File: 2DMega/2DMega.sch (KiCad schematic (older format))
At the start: 41 parts, among them J1 Conn_01x06_Male, J2 Conn_01x06_Female, J3 Conn_02x03_Odd_Even, J4 Conn_01x06_Male, J5 Conn_01x06_Female, P1 Power, P10 CONN_01X01, P11 CONN_01X01, P12 CONN_01X01, P13 CONN_01X01, P2 Analog, P3 Analog, P4 Digital, P5 PWM, P6 PWM, P7 Communication, P8 CONN_01X01, P9 CONN_01X01, U1 SC39-11YWA

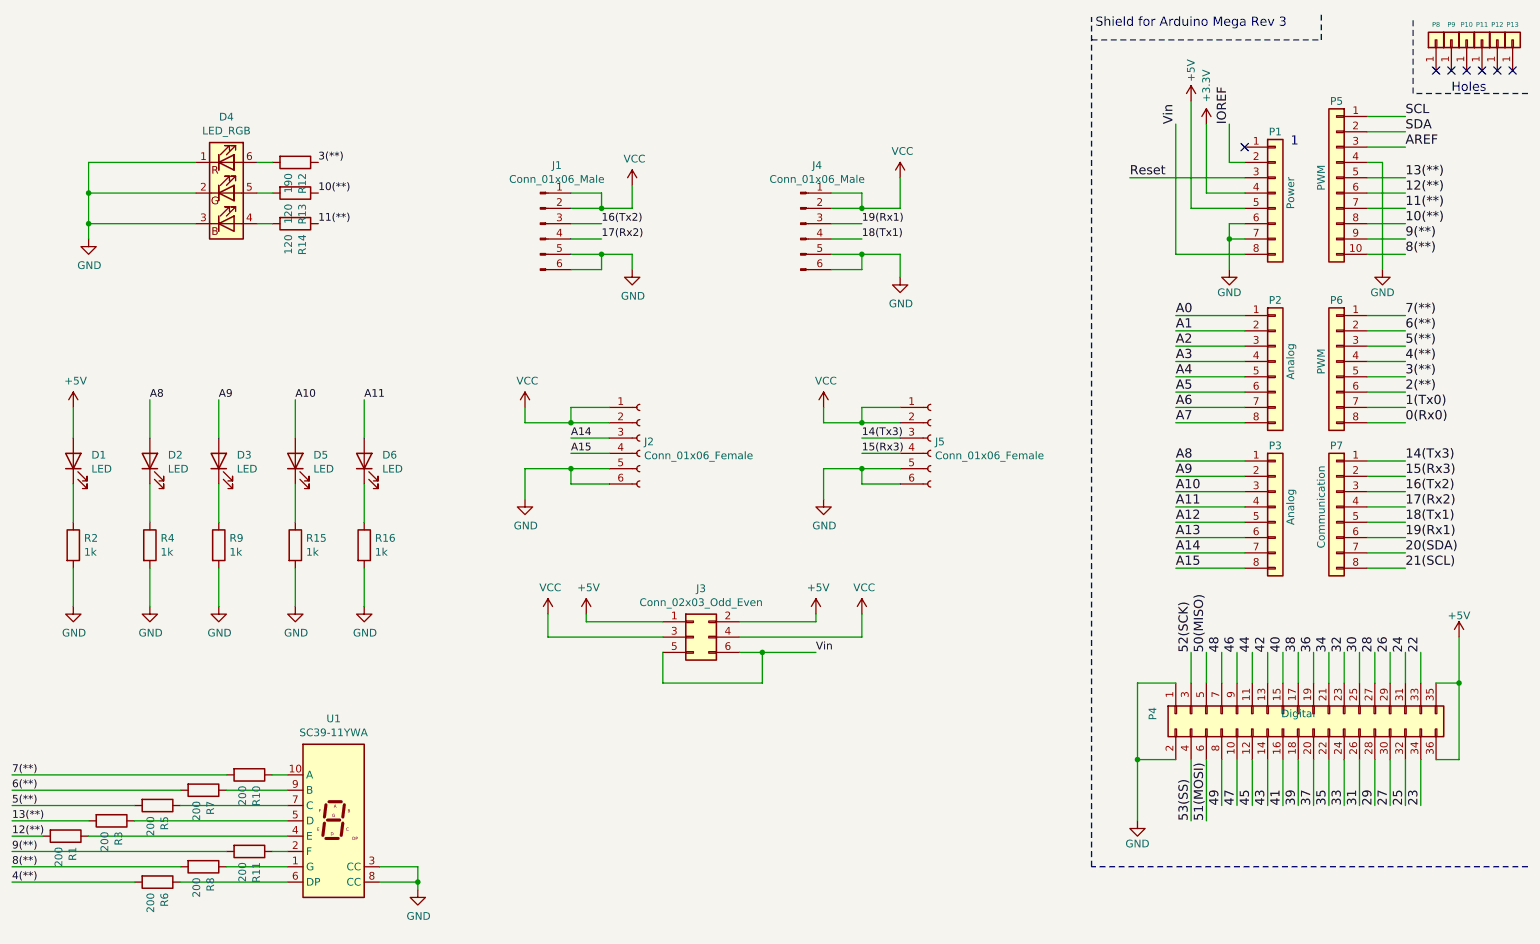
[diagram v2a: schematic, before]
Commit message: Added button and BOM
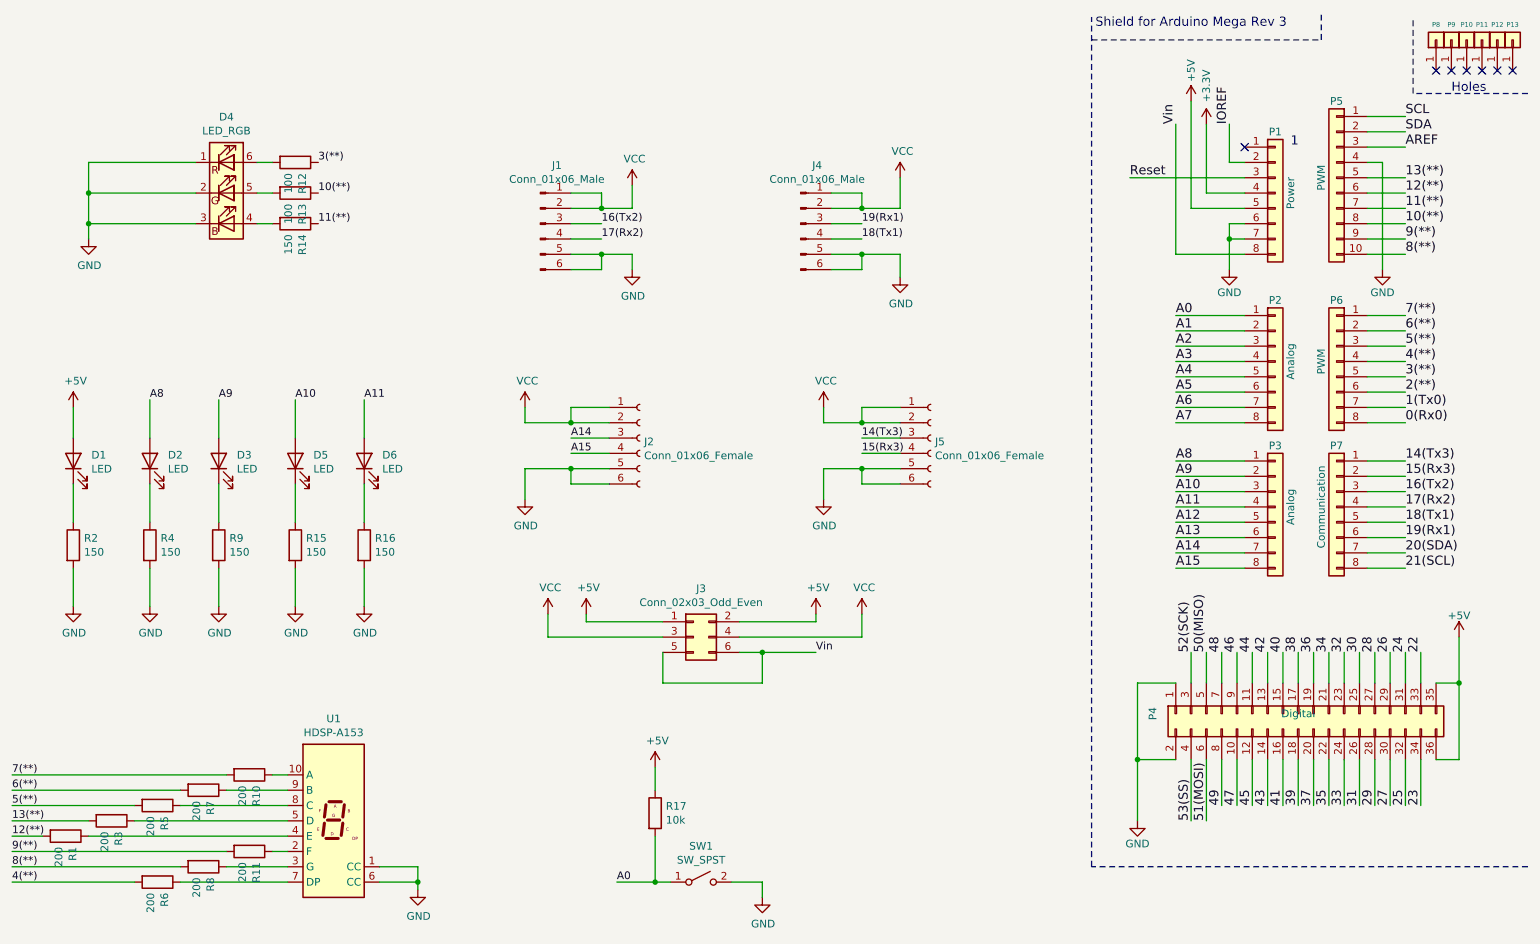
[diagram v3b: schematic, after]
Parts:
- removed U1: SC39-11YWA, Display_7Segment:Sx39-1xxxxx, symbol Display_Character:SC39-11YWA
- added R17: 10k, Resistor_SMD:R_0805_2012Metric_Pad1.20x1.40mm_HandSolder, symbol Device:R
- added SW1: SW_SPST, Button_Switch_SMD:SW_SPST_B3S-1000, symbol Switch:SW_SPST
- added U1: HDSP-A153, Display_7Segment:Sx39-1xxxxx, symbol Display_Character:HDSP-A153
- R12: value 190 -> 100
- R13: value 120 -> 100
- R14: value 120 -> 150
- R15, R16, R2, R4, R9: value 1k -> 150
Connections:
- net +5V: now also R17.1
- net A0: now also R17.2, SW1.1 (A)
- net GND: now also SW1.2 (B), U1.1 (CC), U1.6 (CC)
- net at R10.1: now also U1.10 (A)
- net at R5.1: now also U1.8 (C)
- net at R7.1: now also U1.9 (B)
- net at R3.1: now also U1.5 (D)
- net at R1.1: now also U1.4 (E)
- net at R11.1: now also U1.2 (F)
- net at R8.1: now also U1.3 (G)
- net at R6.1: now also U1.7 (DP)
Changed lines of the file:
@@
 1
 $Comp
-L power:+3V3 #PWR023
+L power:+3V3 #PWR025
 U 1 1 56D71AA9
 P 9100 1200
-F 0 "#PWR023" H 9100 1050 50  0001 C CNN
+F 0 "#PWR025" H 9100 1050 50  0001 C CNN
 F 1 "+3.3V" V 9100 1450 50  0000 C CNN
 F 2 "" H 9100 1200 50  0000 C CNN
@@
 Reset
 $Comp
-L power:+5V #PWR022
+L power:+5V #PWR024
 U 1 1 56D71D10
 P 9000 1050
-F 0 "#PWR022" H 9000 900 50  0001 C CNN
+F 0 "#PWR024" H 9000 900 50  0001 C CNN
 F 1 "+5V" V 9000 1250 50  0000 C CNN
 F 2 "" H 9000 1050 50  0000 C CNN
@@
 $EndComp
 $Comp
-L power:GND #PWR024
+L power:GND #PWR026
 U 1 1 56D721E6
 P 9250 2150
-F 0 "#PWR024" H 9250 1900 50  0001 C CNN
+F 0 "#PWR026" H 9250 1900 50  0001 C CNN
 F 1 "GND" H 9250 2000 50  0000 C CNN
 F 2 "" H 9250 2150 50  0000 C CNN
@@
 $EndComp
 $Comp
-L power:GND #PWR025
+L power:GND #PWR027
 U 1 1 56D72A3D
 P 10250 2150
-F 0 "#PWR025" H 10250 1900 50  0001 C CNN
+F 0 "#PWR027" H 10250 1900 50  0001 C CNN
 F 1 "GND" H 10250 2000 50  0000 C CNN
 F 2 "" H 10250 2150 50  0000 C CNN
@@
 	8900 4850 8650 4850
 $Comp
-L power:GND #PWR021
+L power:GND #PWR023
 U 1 1 56D758F6
 P 8650 5750
-F 0 "#PWR021" H 8650 5500 50  0001 C CNN
+F 0 "#PWR023" H 8650 5500 50  0001 C CNN
 F 1 "GND" H 8650 5600 50  0000 C CNN
 F 2 "" H 8650 5750 50  0000 C CNN
@@
 	10750 4850 10600 4850
 $Comp
-L power:+5V #PWR026
+L power:+5V #PWR028
 U 1 1 56D75AB8
 P 10750 4550
-F 0 "#PWR026" H 10750 4400 50  0001 C CNN
+F 0 "#PWR028" H 10750 4400 50  0001 C CNN
 F 1 "+5V" H 10750 4690 50  0000 C CNN
 F 2 "" H 10750 4550 50  0000 C CNN
@@
 $EndComp
 $Comp
-L power:GND #PWR020
+L power:GND #PWR022
 U 1 1 61023FC6
 P 7100 2200
-F 0 "#PWR020" H 7100 1950 50  0001 C CNN
+F 0 "#PWR022" H 7100 1950 50  0001 C CNN
 F 1 "GND" H 7105 2027 50  0000 C CNN
 F 2 "" H 7100 2200 50  0001 C CNN
@@
 $EndComp
 $Comp
-L power:GND #PWR017
+L power:GND #PWR019
 U 1 1 61025494
 P 6600 3650
-F 0 "#PWR017" H 6600 3400 50  0001 C CNN
+F 0 "#PWR019" H 6600 3400 50  0001 C CNN
 F 1 "GND" H 6605 3477 50  0000 C CNN
 F 2 "" H 6600 3650 50  0001 C CNN
@@
 P 1700 3950
 F 0 "R2" H 1770 3996 50  0000 L CNN
-F 1 "1k" H 1770 3905 50  0000 L CNN
+F 1 "150" H 1770 3905 50  0000 L CNN
 F 2 "Resistor_SMD:R_0805_2012Metric_Pad1.20x1.40mm_HandSolder" V 1630 3950 50  0001 C CNN
 F 3 "~" H 1700 3950 50  0001 C CNN
@@
 P 2200 3950
 F 0 "R4" H 2270 3996 50  0000 L CNN
-F 1 "1k" H 2270 3905 50  0000 L CNN
+F 1 "150" H 2270 3905 50  0000 L CNN
 F 2 "Resistor_SMD:R_0805_2012Metric_Pad1.20x1.40mm_HandSolder" V 2130 3950 50  0001 C CNN
 F 3 "~" H 2200 3950 50  0001 C CNN
@@
 P 2650 3950
 F 0 "R9" H 2720 3996 50  0000 L CNN
-F 1 "1k" H 2720 3905 50  0000 L CNN
+F 1 "150" H 2720 3905 50  0000 L CNN
 F 2 "Resistor_SMD:R_0805_2012Metric_Pad1.20x1.40mm_HandSolder" V 2580 3950 50  0001 C CNN
 F 3 "~" H 2650 3950 50  0001 C CNN
@@
 P 3150 3950
 F 0 "R15" H 3220 3996 50  0000 L CNN
-F 1 "1k" H 3220 3905 50  0000 L CNN
+F 1 "150" H 3220 3905 50  0000 L CNN
 F 2 "Resistor_SMD:R_0805_2012Metric_Pad1.20x1.40mm_HandSolder" V 3080 3950 50  0001 C CNN
 F 3 "~" H 3150 3950 50  0001 C CNN
@@
 P 3600 3950
 F 0 "R16" H 3670 3996 50  0000 L CNN
-F 1 "1k" H 3670 3905 50  0000 L CNN
+F 1 "150" H 3670 3905 50  0000 L CNN
 F 2 "Resistor_SMD:R_0805_2012Metric_Pad1.20x1.40mm_HandSolder" V 3530 3950 50  0001 C CNN
 F 3 "~" H 3600 3950 50  0001 C CNN
@@
 Wire Wire Line
 	2100 5650 1300 5650
-$Comp
-L Display_Character:SC39-11YWA U1
-U 1 1 611BBB20
-P 3400 5750
-F 0 "U1" H 3400 6417 50  0000 C CNN
-F 1 "SC39-11YWA" H 3400 6326 50  0000 C CNN
-F 2 "Display_7Segment:Sx39-1xxxxx" H 3400 5200 50  0001 C CNN
-F 3 "http://www.kingbrightusa.com/images/catalog/SPEC/sc39-11ywa.pdf" H 3400 5750 50  0001 C CNN
-	1    3400 5750
-	1    0    0    -1
-$EndComp
 Text Label 1300 5750 0    50   ~ 0
 13(**)
@@
 $EndComp
 $Comp
-L power:VCC #PWR016
+L power:VCC #PWR018
 U 1 1 6121536E
 P 6600 3050
-F 0 "#PWR016" H 6600 2900 50  0001 C CNN
+F 0 "#PWR018" H 6600 2900 50  0001 C CNN
 F 1 "VCC" H 6615 3223 50  0000 C CNN
 F 2 "" H 6600 3050 50  0001 C CNN
@@
 $EndComp
 $Comp
-L power:VCC #PWR019
+L power:VCC #PWR021
 U 1 1 6121584B
 P 7100 1550
-F 0 "#PWR019" H 7100 1400 50  0001 C CNN
+F 0 "#PWR021" H 7100 1400 50  0001 C CNN
 F 1 "VCC" H 7115 1723 50  0000 C CNN
 F 2 "" H 7100 1550 50  0001 C CNN
@@
 $EndComp
 $Comp
-L power:VCC #PWR018
+L power:VCC #PWR020
 U 1 1 61216BBE
 P 6850 4400
-F 0 "#PWR018" H 6850 4250 50  0001 C CNN
+F 0 "#PWR020" H 6850 4250 50  0001 C CNN
 F 1 "VCC" H 6865 4573 50  0000 C CNN
 F 2 "" H 6850 4400 50  0001 C CNN
@@
 $EndComp
 $Comp
-L power:+5V #PWR015
+L power:+5V #PWR017
 U 1 1 612174B9
 P 6550 4400
-F 0 "#PWR015" H 6550 4250 50  0001 C CNN
+F 0 "#PWR017" H 6550 4250 50  0001 C CNN
 F 1 "+5V" H 6565 4573 50  0000 C CNN
 F 2 "" H 6550 4400 50  0001 C CNN
@@
 P 3150 1450
 F 0 "R12" H 3220 1496 50  0000 L CNN
-F 1 "190" H 3220 1405 50  0000 L CNN
+F 1 "100" H 3220 1405 50  0000 L CNN
 F 2 "Resistor_SMD:R_0805_2012Metric_Pad1.20x1.40mm_HandSolder" V 3080 1450 50  0001 C CNN
 F 3 "~" H 3150 1450 50  0001 C CNN
@@
 P 3150 1650
 F 0 "R13" H 3220 1696 50  0000 L CNN
-F 1 "120" H 3220 1605 50  0000 L CNN
+F 1 "100" H 3220 1605 50  0000 L CNN
 F 2 "Resistor_SMD:R_0805_2012Metric_Pad1.20x1.40mm_HandSolder" V 3080 1650 50  0001 C CNN
 F 3 "~" H 3150 1650 50  0001 C CNN
@@
 P 3150 1850
 F 0 "R14" H 3220 1896 50  0000 L CNN
-F 1 "120" H 3220 1805 50  0000 L CNN
+F 1 "150" H 3220 1805 50  0000 L CNN
 F 2 "Resistor_SMD:R_0805_2012Metric_Pad1.20x1.40mm_HandSolder" V 3080 1850 50  0001 C CNN
 F 3 "~" H 3150 1850 50  0001 C CNN
@@
 Wire Wire Line
 	1800 1650 1800 1850
+$Comp
+L Display_Character:HDSP-A153 U1
+U 1 1 611E1220
+P 3400 5750
+F 0 "U1" H 3400 6417 50  0000 C CNN
+F 1 "HDSP-A153" H 3400 6326 50  0000 C CNN
+F 2 "Display_7Segment:Sx39-1xxxxx" H 3400 5200 50  0001 C CNN
+F 3 "https://docs.broadcom.com/docs/AV02-2553EN" H 3000 6300 50  0001 C CNN
+	1    3400 5750
+	1    0    0    -1
+$EndComp
+$Comp
+L Switch:SW_SPST SW1
+U 1 1 611F57CB
+P 5800 6150
+F 0 "SW1" H 5800 6385 50  0000 C CNN
+F 1 "SW_SPST" H 5800 6294 50  0000 C CNN
+F 2 "Button_Switch_SMD:SW_SPST_B3S-1000" H 5800 6150 50  0001 C CNN
+F 3 "~" H 5800 6150 50  0001 C CNN
+	1    5800 6150
+	1    0    0    -1
+$EndComp
+$Comp
+L Device:R R17
+U 1 1 611F5F08
+P 5500 5700
+F 0 "R17" H 5570 5746 50  0000 L CNN
+F 1 "10k" H 5570 5655 50  0000 L CNN
+F 2 "Resistor_SMD:R_0805_2012Metric_Pad1.20x1.40mm_HandSolder" V 5430 5700 50  0001 C CNN
+F 3 "~" H 5500 5700 50  0001 C CNN
+	1    5500 5700
+	1    0    0    -1
+$EndComp
+$Comp
+L power:+5V #PWR015
+U 1 1 611F6516
+P 5500 5400
+F 0 "#PWR015" H 5500 5250 50  0001 C CNN
+F 1 "+5V" H 5515 5573 50  0000 C CNN
+F 2 "" H 5500 5400 50  0001 C CNN
+F 3 "" H 5500 5400 50  0001 C CNN
+	1    5500 5400
+	1    0    0    -1
+$EndComp
+$Comp
+L power:GND #PWR016
+U 1 1 611F6C97
+P 6200 6250
+F 0 "#PWR016" H 6200 6000 50  0001 C CNN
+F 1 "GND" H 6205 6077 50  0000 C CNN
+F 2 "" H 6200 6250 50  0001 C CNN
+F 3 "" H 6200 6250 50  0001 C CNN
+	1    6200 6250
+	1    0    0    -1
+$EndComp
+Wire Wire Line
+	5600 6150 5500 6150
+Text Label 5250 6150 0    50   ~ 0
+A0
+Wire Wire Line
+	5500 5850 5500 6150
+Connection ~ 5500 6150
+Wire Wire Line
+	5500 6150 5250 6150
+Wire Wire Line
+	5500 5550 5500 5400
+Wire Wire Line
+	6000 6150 6200 6150
+Wire Wire Line
+	6200 6150 6200 6250
 $EndSCHEMATC

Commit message: Added resistors to tx and rx pins, silkscreen tags
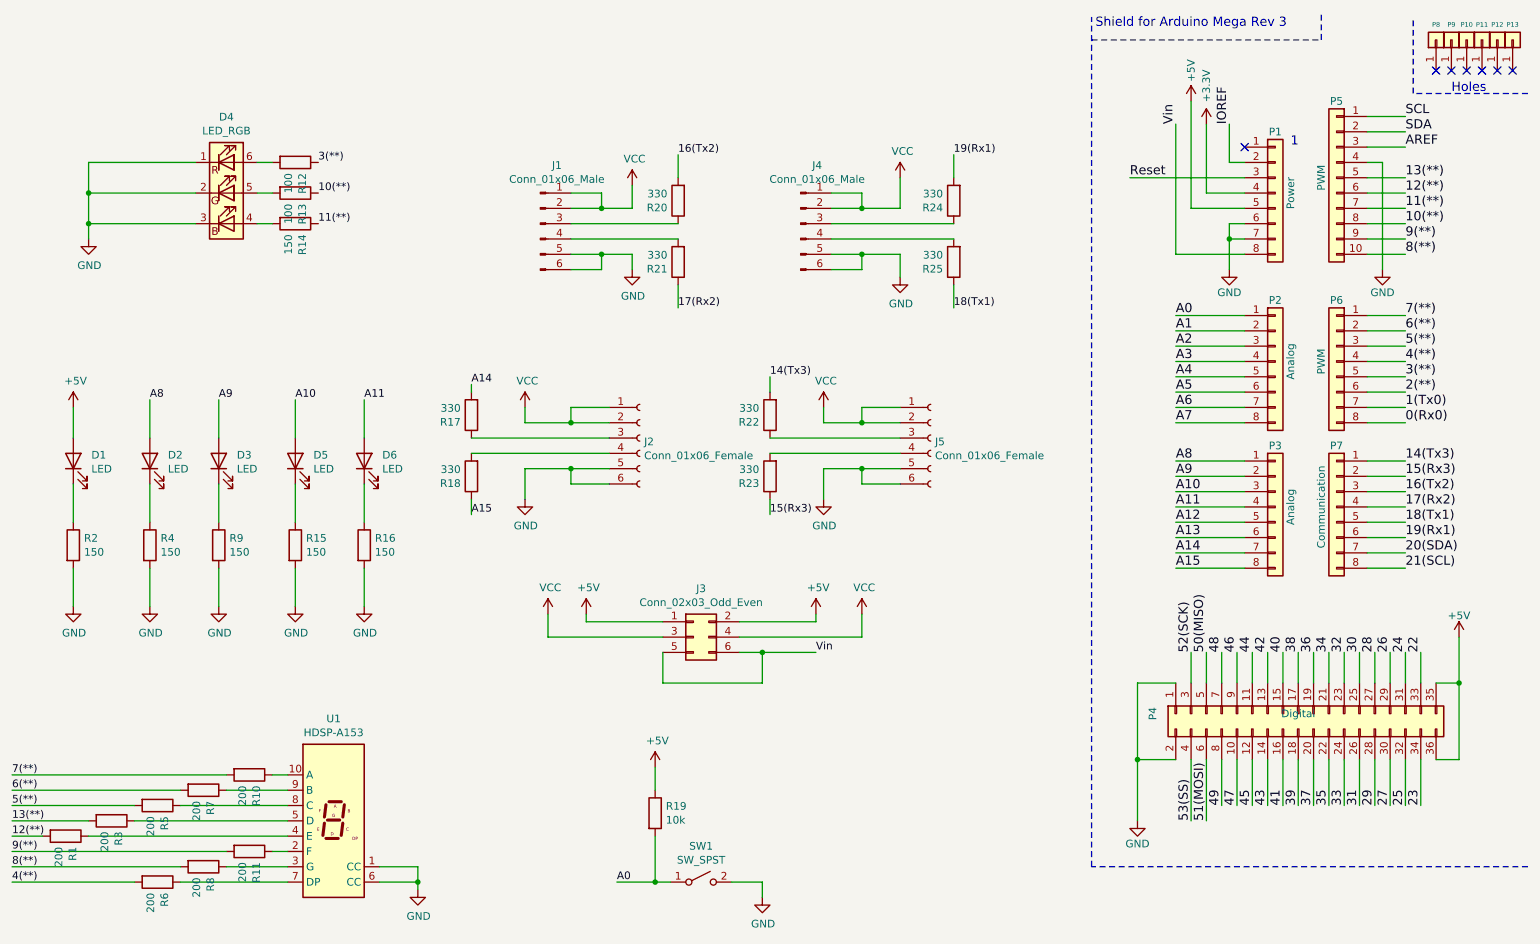
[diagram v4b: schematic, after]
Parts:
- added R17, R18, R20, R21, R22, R23, R24, R25: 330, Resistor_SMD:R_0805_2012Metric_Pad1.20x1.40mm_HandSolder, symbol Device:R
- renumbered R17 to R19
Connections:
- net 14(Tx3): now also R22.2; no longer J5.3 (Pin_3)
- net 15(Rx3): now also R23.1; no longer J5.4 (Pin_4)
- net 16(Tx2): now also R20.2; no longer J1.3 (Pin_3)
- net 17(Rx2): now also R21.1; no longer J1.4 (Pin_4)
- net 18(Tx1): now also R25.1; no longer J4.4 (Pin_4)
- net 19(Rx1): now also R24.2; no longer J4.3 (Pin_3)
- net A14: now also R17.2; no longer J2.3 (Pin_3)
- net A15: now also R18.1; no longer J2.4 (Pin_4)
- new net: J1.3 (Pin_3), R20.1
- new net: J1.4 (Pin_4), R21.2
- new net: J2.3 (Pin_3), R17.1
- new net: J2.4 (Pin_4), R18.2
- new net: J5.3 (Pin_3), R22.1
- new net: J5.4 (Pin_4), R23.2
- new net: J4.3 (Pin_3), R24.1
- new net: J4.4 (Pin_4), R25.2
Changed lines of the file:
@@
 Wire Notes Line
 	8350 6050 8350 500
-Wire Wire Line
-	4950 1850 5150 1850
-Wire Wire Line
-	4950 1950 5150 1950
-Wire Wire Line
-	6650 1850 6850 1850
-Wire Wire Line
-	6650 1950 6850 1950
-Wire Wire Line
-	5200 3250 4950 3250
-Wire Wire Line
-	5200 3350 4950 3350
-Wire Wire Line
-	7100 3250 6850 3250
-Wire Wire Line
-	7100 3350 6850 3350
 $Comp
 L power:GND #PWR014
@@
 Wire Wire Line
 	4650 3450 4950 3450
-Text Label 6850 1950 0    50   ~ 0
+Text Label 7450 2400 0    50   ~ 0
 18(Tx1)
-Text Label 6850 1850 0    50   ~ 0
+Text Label 7450 1400 0    50   ~ 0
 19(Rx1)
-Text Label 5150 1850 0    50   ~ 0
+Text Label 5650 1400 0    50   ~ 0
 16(Tx2)
-Text Label 5150 1950 0    50   ~ 0
+Text Label 5650 2400 0    50   ~ 0
 17(Rx2)
-Text Label 6850 3250 0    50   ~ 0
+Text Label 6250 2850 0    50   ~ 0
 14(Tx3)
-Text Label 6850 3350 0    50   ~ 0
+Text Label 6250 3750 0    50   ~ 0
 15(Rx3)
 $Comp
@@
 	0    1    1    0
 $EndComp
-Text Label 4950 3250 0    50   ~ 0
+Text Label 4300 2900 0    50   ~ 0
 A14
-Text Label 4950 3350 0    50   ~ 0
+Text Label 4300 3750 0    50   ~ 0
 A15
 Text Label 3300 1450 0    50   ~ 0
@@
 $EndComp
 $Comp
-L Device:R R17
+L Device:R R19
 U 1 1 611F5F08
 P 5500 5700
-F 0 "R17" H 5570 5746 50  0000 L CNN
+F 0 "R19" H 5570 5746 50  0000 L CNN
 F 1 "10k" H 5570 5655 50  0000 L CNN
 F 2 "Resistor_SMD:R_0805_2012Metric_Pad1.20x1.40mm_HandSolder" V 5430 5700 50  0001 C CNN
@@
 Wire Wire Line
 	6200 6150 6200 6250
+$Comp
+L Device:R R20
+U 1 1 6125EDCE
+P 5650 1700
+F 0 "R20" H 5720 1746 50  0000 L CNN
+F 1 "330" H 5720 1655 50  0000 L CNN
+F 2 "Resistor_SMD:R_0805_2012Metric_Pad1.20x1.40mm_HandSolder" V 5580 1700 50  0001 C CNN
+F 3 "~" H 5650 1700 50  0001 C CNN
+	1    5650 1700
+	-1   0    0    1
+$EndComp
+$Comp
+L Device:R R21
+U 1 1 61260325
+P 5650 2100
+F 0 "R21" H 5720 2146 50  0000 L CNN
+F 1 "330" H 5720 2055 50  0000 L CNN
+F 2 "Resistor_SMD:R_0805_2012Metric_Pad1.20x1.40mm_HandSolder" V 5580 2100 50  0001 C CNN
+F 3 "~" H 5650 2100 50  0001 C CNN
+	1    5650 2100
+	-1   0    0    1
+$EndComp
+$Comp
+L Device:R R25
+U 1 1 61260660
+P 7450 2100
+F 0 "R25" H 7520 2146 50  0000 L CNN
+F 1 "330" H 7520 2055 50  0000 L CNN
+F 2 "Resistor_SMD:R_0805_2012Metric_Pad1.20x1.40mm_HandSolder" V 7380 2100 50  0001 C CNN
+F 3 "~" H 7450 2100 50  0001 C CNN
+	1    7450 2100
+	-1   0    0    1
+$EndComp
+$Comp
+L Device:R R24
+U 1 1 61260BD4
+P 7450 1700
+F 0 "R24" H 7520 1746 50  0000 L CNN
+F 1 "330" H 7520 1655 50  0000 L CNN
+F 2 "Resistor_SMD:R_0805_2012Metric_Pad1.20x1.40mm_HandSolder" V 7380 1700 50  0001 C CNN
+F 3 "~" H 7450 1700 50  0001 C CNN
+	1    7450 1700
+	-1   0    0    1
+$EndComp
+$Comp
+L Device:R R17
+U 1 1 61260FAB
+P 4300 3100
+F 0 "R17" H 4370 3146 50  0000 L CNN
+F 1 "330" H 4370 3055 50  0000 L CNN
+F 2 "Resistor_SMD:R_0805_2012Metric_Pad1.20x1.40mm_HandSolder" V 4230 3100 50  0001 C CNN
+F 3 "~" H 4300 3100 50  0001 C CNN
+	1    4300 3100
+	-1   0    0    1
+$EndComp
+$Comp
+L Device:R R18
+U 1 1 6126FA4C
+P 4300 3500
+F 0 "R18" H 4370 3546 50  0000 L CNN
+F 1 "330" H 4370 3455 50  0000 L CNN
+F 2 "Resistor_SMD:R_0805_2012Metric_Pad1.20x1.40mm_HandSolder" V 4230 3500 50  0001 C CNN
+F 3 "~" H 4300 3500 50  0001 C CNN
+	1    4300 3500
+	-1   0    0    1
+$EndComp
+Wire Wire Line
+	4950 1850 5650 1850
+Wire Wire Line
+	4950 1950 5650 1950
+Wire Wire Line
+	5650 1550 5650 1400
+Wire Wire Line
+	5650 2250 5650 2400
+Wire Wire Line
+	6650 1850 7450 1850
+Wire Wire Line
+	6650 1950 7450 1950
+Wire Wire Line
+	7450 2250 7450 2400
+Wire Wire Line
+	7450 1550 7450 1400
+Wire Wire Line
+	4300 3250 5200 3250
+Wire Wire Line
+	4300 2950 4300 2900
+Wire Wire Line
+	4300 3350 5200 3350
+Wire Wire Line
+	4300 3650 4300 3750
+$Comp
+L Device:R R22
+U 1 1 61340794
+P 6250 3100
+F 0 "R22" H 6320 3146 50  0000 L CNN
+F 1 "330" H 6320 3055 50  0000 L CNN
+F 2 "Resistor_SMD:R_0805_2012Metric_Pad1.20x1.40mm_HandSolder" V 6180 3100 50  0001 C CNN
+F 3 "~" H 6250 3100 50  0001 C CNN
+	1    6250 3100
+	-1   0    0    1
+$EndComp
+$Comp
+L Device:R R23
+U 1 1 61341479
+P 6250 3500
+F 0 "R23" H 6320 3546 50  0000 L CNN
+F 1 "330" H 6320 3455 50  0000 L CNN
+F 2 "Resistor_SMD:R_0805_2012Metric_Pad1.20x1.40mm_HandSolder" V 6180 3500 50  0001 C CNN
+F 3 "~" H 6250 3500 50  0001 C CNN
+	1    6250 3500
+	-1   0    0    1
+$EndComp
+Wire Wire Line
+	6250 3650 6250 3750
+Wire Wire Line
+	6250 3350 7100 3350
+Wire Wire Line
+	6250 3250 7100 3250
+Wire Wire Line
+	6250 2950 6250 2850
 $EndSCHEMATC
